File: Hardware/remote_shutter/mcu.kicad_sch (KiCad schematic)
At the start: 31 parts, among them J4 Buzzer, U2 ESP32-PICO-MINI-02, Y1 NX3215SA-32.768K-STD-MUA-14

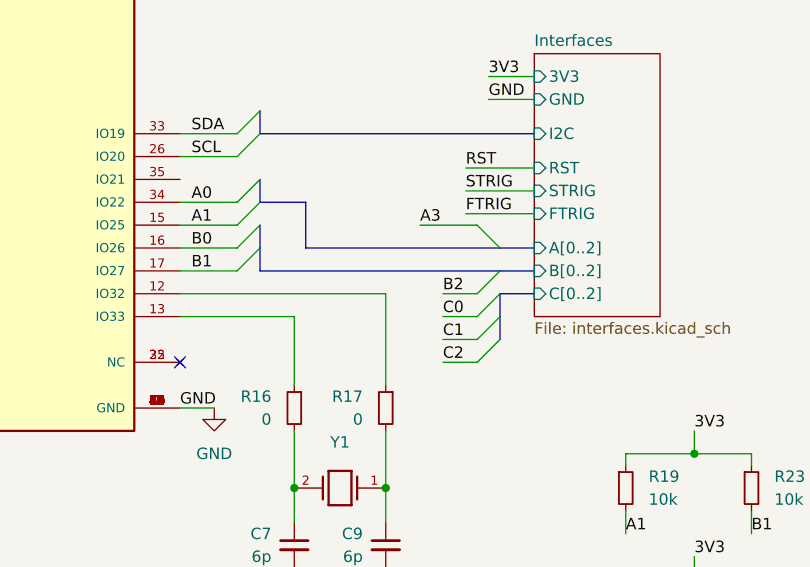
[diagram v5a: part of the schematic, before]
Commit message: Replaced rotary encoders
Now one flat to save space.
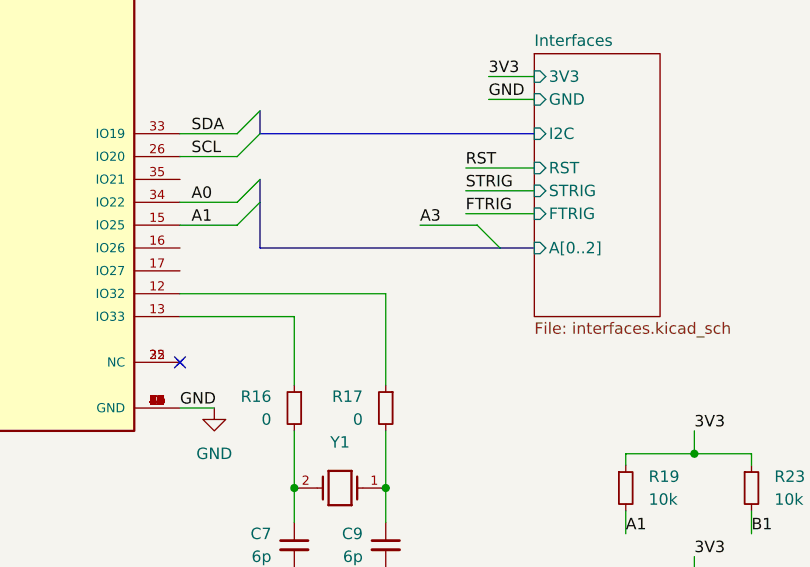
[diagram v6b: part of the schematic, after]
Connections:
- net B1: no longer U2.17 (IO27)
- net B0: no longer names the net of U2.16 (IO26)
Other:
- sheet Interfaces ports: added none; removed B[0..2], C[0..2]
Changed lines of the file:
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@@
-    (stroke (width 0) (type default) (color 0 0 0 0))
-  )
-  (bus_entry (at 184.15 99.06) (size 2.54 -2.54)
-    (stroke (width 0) (type default) (color 0 0 0 0))
-  )
-  (bus_entry (at 157.48 91.44) (size 2.54 -2.54)
     (stroke (width 0) (type default) (color 0 0 0 0))
   )
@@
     (stroke (width 0) (type default) (color 0 0 0 0))
   )
-  (bus_entry (at 157.48 88.9) (size 2.54 -2.54)
-    (stroke (width 0) (type default) (color 0 0 0 0))
-  )
-  (bus_entry (at 184.15 93.98) (size 2.54 -2.54)
-    (stroke (width 0) (type default) (color 0 0 0 0))
-  )
   (bus_entry (at 157.48 78.74) (size 2.54 -2.54)
     (stroke (width 0) (type default) (color 0 0 0 0))
@@
     (stroke (width 0) (type default) (color 0 0 0 0))
   )
-  (bus_entry (at 184.15 96.52) (size 2.54 -2.54)
-    (stroke (width 0) (type default) (color 0 0 0 0))
-  )
-  (bus_entry (at 184.15 101.6) (size 2.54 -2.54)
-    (stroke (width 0) (type default) (color 0 0 0 0))
-  )
   (wire (pts (xy 200.66 111.76) (xy 200.66 113.03))
     (stroke (width 0) (type default) (color 0 0 0 0))
@@
     (stroke (width 0) (type default) (color 0 0 0 0))
   )
-  (bus (pts (xy 160.02 88.9) (xy 160.02 91.44))
-    (stroke (width 0) (type default) (color 0 0 0 0))
-  )
-  (bus (pts (xy 160.02 86.36) (xy 160.02 88.9))
-    (stroke (width 0) (type default) (color 0 0 0 0))
-  )
   (wire (pts (xy 151.13 55.88) (xy 161.29 55.88))
     (stroke (width 0) (type default) (color 0 0 0 0))
@@
     (stroke (width 0) (type default) (color 0 0 0 0))
   )
-  (bus (pts (xy 186.69 96.52) (xy 186.69 93.98))
-    (stroke (width 0) (type default) (color 0 0 0 0))
-  )
   (wire (pts (xy 88.9 58.42) (xy 100.33 58.42))
     (stroke (width 0) (type default) (color 0 0 0 0))
@@
     (stroke (width 0) (type default) (color 0 0 0 0))
   )
-  (bus (pts (xy 160.02 91.44) (xy 186.69 91.44))
-    (stroke (width 0) (type default) (color 0 0 0 0))
-  )
   (wire (pts (xy 177.8 86.36) (xy 184.15 86.36))
     (stroke (width 0) (type default) (color 0 0 0 0))
@@
     (stroke (width 0) (type default) (color 0 0 0 0))
   )
-  (bus (pts (xy 165.1 88.9) (xy 186.69 88.9))
+  (bus (pts (xy 160.02 88.9) (xy 186.69 88.9))
     (stroke (width 0) (type default) (color 0 0 0 0))
   )
@@
     (stroke (width 0) (type default) (color 0 0 0 0))
   )
-  (bus (pts (xy 160.02 83.82) (xy 165.1 83.82))
-    (stroke (width 0) (type default) (color 0 0 0 0))
-  )
   (wire (pts (xy 95.25 157.48) (xy 95.25 160.02))
     (stroke (width 0) (type default) (color 0 0 0 0))
   )
-  (wire (pts (xy 180.34 101.6) (xy 184.15 101.6))
-    (stroke (width 0) (type default) (color 0 0 0 0))
-  )
   (wire (pts (xy 129.54 161.29) (xy 129.54 152.4))
     (stroke (width 0) (type default) (color 0 0 0 0))
   )
-  (bus (pts (xy 186.69 91.44) (xy 190.5 91.44))
-    (stroke (width 0) (type default) (color 0 0 0 0))
-  )
   (wire (pts (xy 106.68 62.23) (xy 106.68 66.04))
     (stroke (width 0) (type default) (color 0 0 0 0))
   )
-  (wire (pts (xy 180.34 93.98) (xy 184.15 93.98))
-    (stroke (width 0) (type default) (color 0 0 0 0))
-  )
   (wire (pts (xy 88.9 78.74) (xy 95.25 78.74))
     (stroke (width 0) (type default) (color 0 0 0 0))
@@
     (stroke (width 0) (type default) (color 0 0 0 0))
   )
-  (wire (pts (xy 151.13 91.44) (xy 157.48 91.44))
-    (stroke (width 0) (type default) (color 0 0 0 0))
-  )
   (wire (pts (xy 151.13 86.36) (xy 157.48 86.36))
     (stroke (width 0) (type default) (color 0 0 0 0))
@@
     (stroke (width 0) (type default) (color 0 0 0 0))
   )
-  (bus (pts (xy 186.69 93.98) (xy 190.5 93.98))
-    (stroke (width 0) (type default) (color 0 0 0 0))
-  )
   (wire (pts (xy 116.84 86.36) (xy 120.65 86.36))
     (stroke (width 0) (type default) (color 0 0 0 0))
@@
     (stroke (width 0) (type default) (color 0 0 0 0))
   )
-  (bus (pts (xy 165.1 83.82) (xy 165.1 88.9))
+  (bus (pts (xy 160.02 83.82) (xy 160.02 88.9))
     (stroke (width 0) (type default) (color 0 0 0 0))
   )
@@
     (stroke (width 0) (type default) (color 0 0 0 0))
   )
-  (wire (pts (xy 180.34 99.06) (xy 184.15 99.06))
-    (stroke (width 0) (type default) (color 0 0 0 0))
-  )
   (wire (pts (xy 114.3 93.98) (xy 120.65 93.98))
     (stroke (width 0) (type default) (color 0 0 0 0))
@@
     (stroke (width 0) (type default) (color 0 0 0 0))
   )
-  (wire (pts (xy 151.13 88.9) (xy 157.48 88.9))
-    (stroke (width 0) (type default) (color 0 0 0 0))
-  )
   (wire (pts (xy 214.63 146.05) (xy 214.63 148.59))
     (stroke (width 0) (type default) (color 0 0 0 0))
@@
     (stroke (width 0) (type default) (color 0 0 0 0))
   )
-  (wire (pts (xy 180.34 96.52) (xy 184.15 96.52))
-    (stroke (width 0) (type default) (color 0 0 0 0))
-  )
   (wire (pts (xy 151.13 78.74) (xy 157.48 78.74))
     (stroke (width 0) (type default) (color 0 0 0 0))
@@
     (stroke (width 0) (type default) (color 0 0 0 0))
   )
-  (bus (pts (xy 186.69 96.52) (xy 186.69 99.06))
-    (stroke (width 0) (type default) (color 0 0 0 0))
-  )
   (wire (pts (xy 114.3 99.06) (xy 120.65 99.06))
     (stroke (width 0) (type default) (color 0 0 0 0))
@@
     (effects (font (size 1.27 1.27)) (justify left bottom))
   )
-  (label "B2" (at 180.34 93.98 0)
-    (effects (font (size 1.27 1.27)) (justify left bottom))
-  )
-  (label "B1" (at 152.4 91.44 0)
-    (effects (font (size 1.27 1.27)) (justify left bottom))
-  )
   (label "SCL" (at 204.47 58.42 0)
     (effects (font (size 1.27 1.27)) (justify left bottom))
   )
-  (label "C1" (at 180.34 99.06 0)
-    (effects (font (size 1.27 1.27)) (justify left bottom))
-  )
   (label "3V3" (at 208.28 137.16 0)
     (effects (font (size 1.27 1.27)) (justify left bottom))
@@
     (effects (font (size 1.27 1.27)) (justify left bottom))
   )
-  (label "C2" (at 180.34 101.6 0)
-    (effects (font (size 1.27 1.27)) (justify left bottom))
-  )
   (label "3V3" (at 151.13 45.72 0)
     (effects (font (size 1.27 1.27)) (justify left bottom))
@@
     (effects (font (size 1.27 1.27)) (justify left bottom))
   )
-  (label "B0" (at 152.4 88.9 0)
-    (effects (font (size 1.27 1.27)) (justify left bottom))
-  )
   (label "A2" (at 200.66 134.62 0)
     (effects (font (size 1.27 1.27)) (justify left bottom))
   )
   (label "GND" (at 151.13 106.68 0)
-    (effects (font (size 1.27 1.27)) (justify left bottom))
-  )
-  (label "C0" (at 180.34 96.52 0)
     (effects (font (size 1.27 1.27)) (justify left bottom))
   )
@@
       (effects (font (size 1.27 1.27)) (justify left))
     )
-    (pin "B[0..2]" input (at 190.5 91.44 180)
-      (effects (font (size 1.27 1.27)) (justify left))
-    )
     (pin "I2C" input (at 190.5 76.2 180)
       (effects (font (size 1.27 1.27)) (justify left))
@@
       (effects (font (size 1.27 1.27)) (justify left))
     )
-    (pin "C[0..2]" input (at 190.5 93.98 180)
-      (effects (font (size 1.27 1.27)) (justify left))
-    )

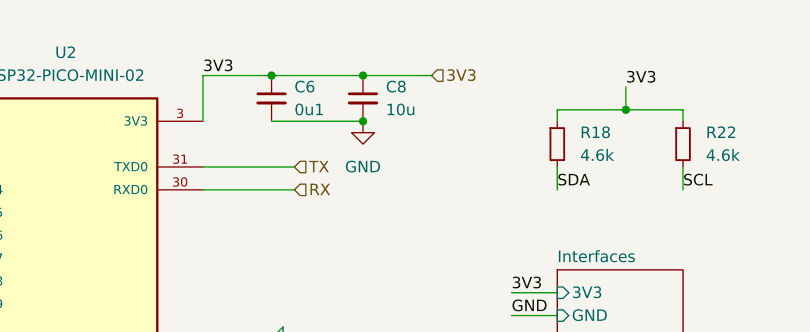
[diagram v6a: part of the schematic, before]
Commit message: Started routing. Added power switch.
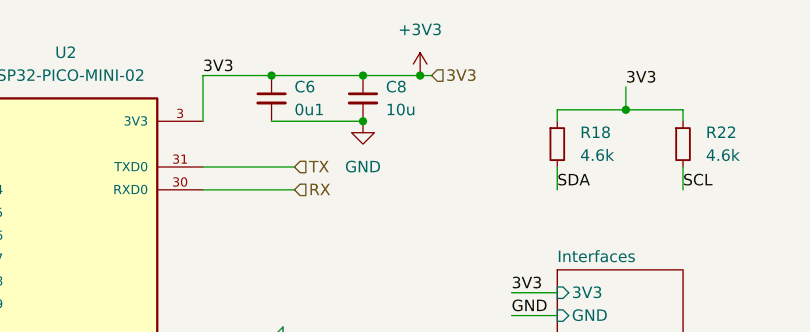
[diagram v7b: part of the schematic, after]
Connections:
- net 3V3 renamed +3V3
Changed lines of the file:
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@@
   (junction (at 198.12 49.53) (diameter 0) (color 0 0 0 0)
+  )
+  (junction (at 175.26 45.72) (diameter 0) (color 0 0 0 0)
   )
   (junction (at 129.54 152.4) (diameter 0) (color 0 0 0 0)
@@
     (stroke (width 0) (type default) (color 0 0 0 0))
   )
-  (wire (pts (xy 176.53 45.72) (xy 168.91 45.72))
+  (wire (pts (xy 176.53 45.72) (xy 175.26 45.72))
     (stroke (width 0) (type default) (color 0 0 0 0))
   )
@@
   )
   (wire (pts (xy 151.13 76.2) (xy 157.48 76.2))
+    (stroke (width 0) (type default) (color 0 0 0 0))
+  )
+  (wire (pts (xy 175.26 45.72) (xy 168.91 45.72))
     (stroke (width 0) (type default) (color 0 0 0 0))
   )
@@
     (pin "2")
   )
+  (symbol (lib_id "power:+3V3") (at 175.26 45.72 0) (unit 1)
+    (in_bom yes) (on_board yes) (fields_autoplaced)
+    (property "Reference" "#PWR?" (id 0) (at 175.26 49.53 0)
+      (effects (font (size 1.27 1.27)) hide)
+    )
+    (property "Value" "+3V3" (id 1) (at 175.26 40.64 0))
+    (property "Footprint" "" (id 2) (at 175.26 45.72 0)
+      (effects (font (size 1.27 1.27)) hide)
+    )
+    (property "Datasheet" "" (id 3) (at 175.26 45.72 0)
+      (effects (font (size 1.27 1.27)) hide)
+    )
+    (pin "1")
+  )
   (symbol (lib_id "Device:R_Small") (at 200.66 143.51 0) (unit 1)
